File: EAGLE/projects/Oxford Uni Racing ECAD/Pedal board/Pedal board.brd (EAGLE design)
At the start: 165.1 x 216.8 mm, 42 parts, among them J1 T821108A1S100CEU, J2 T821108A1S100CEU, J3 T821108A1S100CEU, J4 T821108A1S100CEU, K1 RT444012, T1 BT169, X2 D-SUB9-H2M09ST

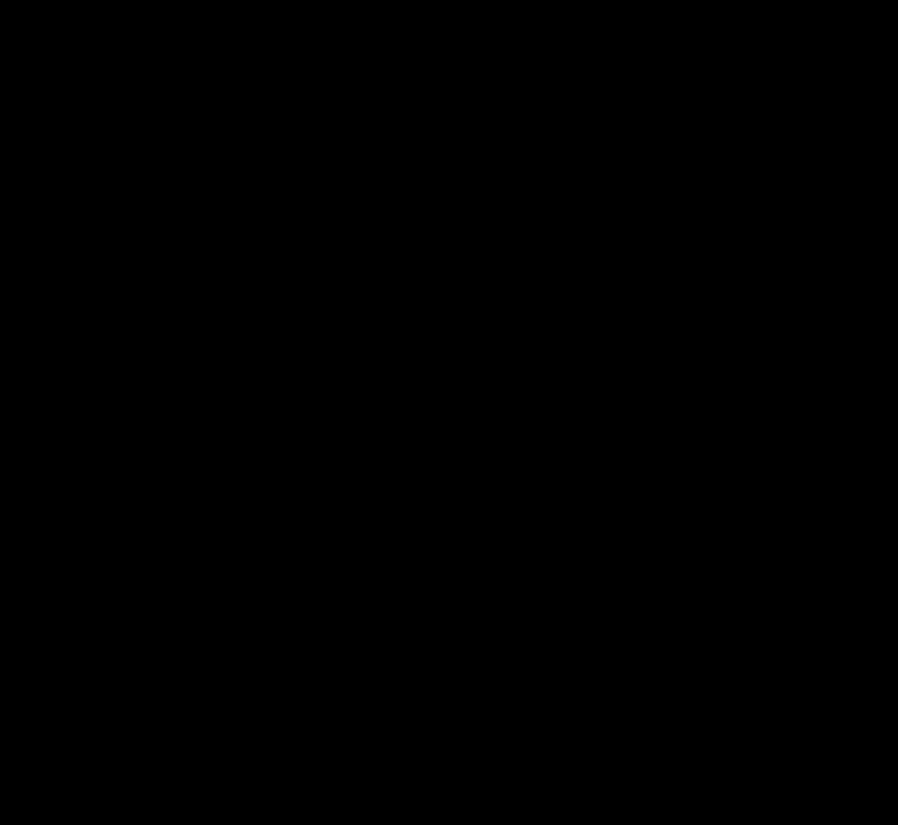
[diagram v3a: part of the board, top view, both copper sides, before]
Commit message: added outut connectors to the pedal board
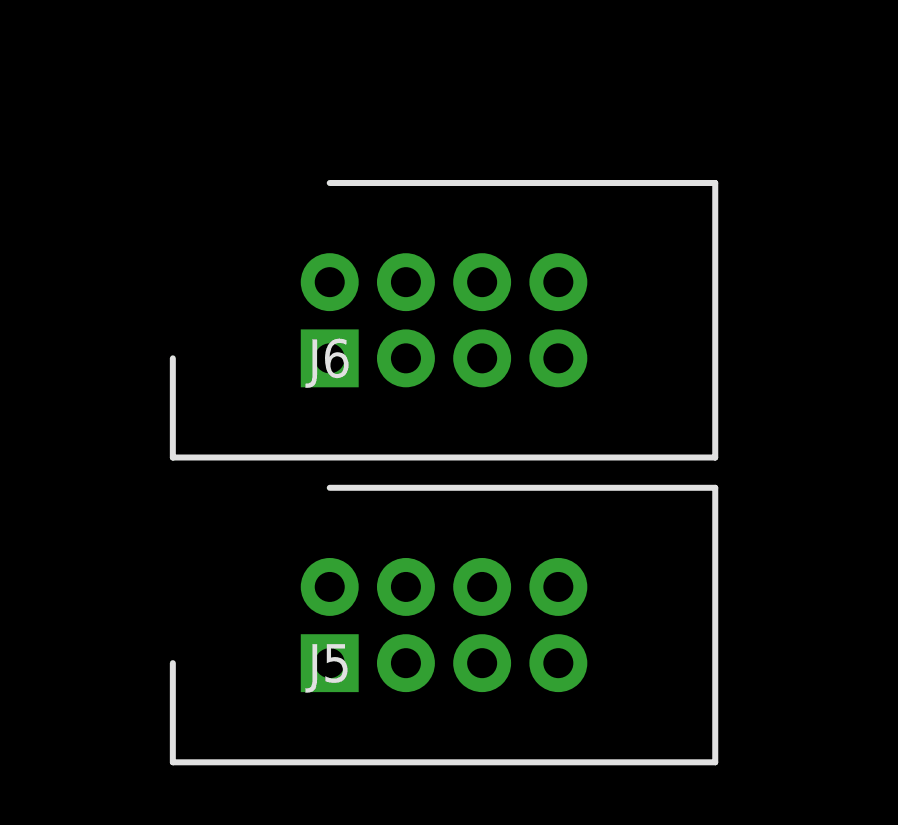
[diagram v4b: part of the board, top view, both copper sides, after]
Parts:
- added J5, J6: T821108A1S100CEU, T821108A1S100CEU:HDRV8W64P254_2X4_1778X895X915P
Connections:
- net CAN_H renamed CANH
- net CAN_L renamed CANL
- new net BRAKE_LIGHT_PWR_OUT: J5.8
- new net BR_POSS: J6.5
- new net BR_PRESS: J6.6
- new net ST_WH_POSS: J6.7
- net 3.3V: now also J6.1
- net 5V: now also J6.2
- net GND: now also J5.3, J6.3
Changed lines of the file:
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@@
 <attribute name="VALUE" x="149.86" y="43.18" size="1.27" layer="27" align="center"/>
+</element>
+<element name="J6" library="T821108A1S100CEU" package="HDRV8W64P254_2X4_1778X895X915P" value="T821108A1S100CEU" x="8.89" y="-120.65" smashed="yes">
+<attribute name="DESCRIPTION" value="HEADER, VERTICAL, 2.54MM, 8WAY Amphenol T821 Series, 2.54mm Pitch 8 Way 2 Row Straight PCB Header, Solder Termination, 3A" x="6.35" y="-120.65" size="1.778" layer="27" display="off"/>
+<attribute name="HEIGHT" value="9.15mm" x="6.35" y="-120.65" size="1.778" layer="27" display="off"/>
+<attribute name="MANUFACTURER_NAME" value="Amphenol" x="6.35" y="-120.65" size="1.778" layer="27" display="off"/>
+<attribute name="MANUFACTURER_PART_NUMBER" value="T821108A1S100CEU" x="6.35" y="-120.65" size="1.778" layer="27" display="off"/>
+<attribute name="NAME" x="8.89" y="-120.65" size="1.27" layer="25" align="center"/>
+<attribute name="RS_PART_NUMBER" value="1702738" x="6.35" y="-120.65" size="1.778" layer="27" display="off"/>
+<attribute name="VALUE" x="8.89" y="-120.65" size="1.27" layer="27" align="center"/>
+</element>
+<element name="J5" library="T821108A1S100CEU" package="HDRV8W64P254_2X4_1778X895X915P" value="T821108A1S100CEU" x="8.89" y="-130.81" smashed="yes">
+<attribute name="DESCRIPTION" value="HEADER, VERTICAL, 2.54MM, 8WAY Amphenol T821 Series, 2.54mm Pitch 8 Way 2 Row Straight PCB Header, Solder Termination, 3A" x="6.35" y="-130.81" size="1.778" layer="27" display="off"/>
+<attribute name="HEIGHT" value="9.15mm" x="6.35" y="-130.81" size="1.778" layer="27" display="off"/>
+<attribute name="MANUFACTURER_NAME" value="Amphenol" x="6.35" y="-130.81" size="1.778" layer="27" display="off"/>
+<attribute name="MANUFACTURER_PART_NUMBER" value="T821108A1S100CEU" x="6.35" y="-130.81" size="1.778" layer="27" display="off"/>
+<attribute name="NAME" x="8.89" y="-130.81" size="1.27" layer="25" align="center"/>
+<attribute name="RS_PART_NUMBER" value="1702738" x="6.35" y="-130.81" size="1.778" layer="27" display="off"/>
+<attribute name="VALUE" x="8.89" y="-130.81" size="1.27" layer="27" align="center"/>
 </element>
 </elements>
@@
 <contactref element="J2" pad="4"/>
 <contactref element="J4" pad="3"/>
+<contactref element="J6" pad="3"/>
+<contactref element="J5" pad="3"/>
+<wire x1="149.86" y1="36.83" x2="149.86" y2="45.72" width="0" layer="19" extent="1-1"/>
+<wire x1="149.86" y1="34.29" x2="149.86" y2="36.83" width="0" layer="19" extent="1-1"/>
+<wire x1="134.62" y1="22.86" x2="149.86" y2="34.29" width="0" layer="19" extent="16-16"/>
 <wire x1="111.76" y1="17.78" x2="125.73" y2="10.16" width="0" layer="19" extent="16-16"/>
-<wire x1="87.63" y1="22.86" x2="102.87" y2="10.16" width="0" layer="19" extent="16-16"/>
+<wire x1="91.44" y1="11.43" x2="102.87" y2="10.16" width="0" layer="19" extent="16-16"/>
 <wire x1="20.6502" y1="-29.72970625" x2="82.55" y2="8.7376" width="0" layer="19" extent="16-16"/>
 <wire x1="19.124928125" y1="-63.86195" x2="19.3294" y2="-37.5412" width="0" layer="19" extent="1-1"/>
 <wire x1="12.75714375" y1="-86.45144375" x2="13.55979375" y2="-86.45144375" width="0" layer="19" extent="16-16"/>
-<wire x1="149.86" y1="36.83" x2="24.63165" y2="-97.547428125" width="0" layer="19" extent="1-1"/>
-<wire x1="149.86" y1="34.29" x2="149.86" y2="36.83" width="0" layer="19" extent="1-1"/>
-<wire x1="149.86" y1="45.72" x2="149.86" y2="34.29" width="0" layer="19" extent="1-1"/>
+<wire x1="11.43" y1="-120.65" x2="24.63165" y2="-97.547428125" width="0" layer="19" extent="1-1"/>
+<wire x1="11.43" y1="-130.81" x2="11.43" y2="-120.65" width="0" layer="19" extent="1-1"/>
 </signal>
 <signal name="N$3">
@@
 <wire x1="111.76" y1="7.62" x2="125.73" y2="7.62" width="0" layer="19" extent="16-16"/>
 <wire x1="90.17" y1="20.32" x2="102.87" y2="7.62" width="0" layer="19" extent="16-16"/>
-<wire x1="23.8506" y1="-31.0388" x2="90.17" y2="20.32" width="0" layer="19" extent="1-1"/>
-<wire x1="11.376653125" y1="-63.733675" x2="23.8506" y2="-31.0388" width="0" layer="19" extent="16-16"/>
-</signal>
-<signal name="CAN_L">
+<wire x1="71.11193125" y1="-68.1202625" x2="102.87" y2="7.62" width="0" layer="19" extent="16-16"/>
+<wire x1="23.8506" y1="-31.0388" x2="11.376653125" y2="-63.733675" width="0" layer="19" extent="16-16"/>
+</signal>
+<signal name="CANL">
 <contactref element="X2" pad="2"/>
 <wire x1="85.09" y1="14.7717375" x2="85.21065" y2="14.6510875" width="0.6096" layer="16"/>
@@
 <wire x1="85.09" y1="20.32" x2="85.09" y2="22.86" width="0" layer="19" extent="1-1"/>
 </signal>
-<signal name="CAN_H">
+<signal name="CANH">
 <contactref element="X2" pad="7"/>
 <wire x1="83.9343" y1="11.5824" x2="82.55" y2="12.9667" width="1.27" layer="16"/>
@@
 <wire x1="137.16" y1="21.59" x2="137.16" y2="22.86" width="1.27" layer="16"/>
 <wire x1="139.7" y1="21.59" x2="137.16" y2="21.59" width="1.27" layer="16"/>
-<wire x1="78.3971" y1="11.5824" x2="137.16" y2="7.62" width="0" layer="19" extent="1-1"/>
+<contactref element="J6" pad="2"/>
+<wire x1="78.3971" y1="11.5824" x2="137.16" y2="15.24" width="0" layer="19" extent="1-1"/>
+<wire x1="8.89" y1="-118.11" x2="78.3971" y2="11.5824" width="0" layer="19" extent="1-1"/>
 </signal>
 <signal name="N$24">
@@
 <wire x1="114.3" y1="21.59" x2="114.3" y2="22.86" width="1.27" layer="16"/>
 <wire x1="116.84" y1="21.59" x2="114.3" y2="21.59" width="1.27" layer="16"/>
-<wire x1="147.32" y1="36.83" x2="114.3" y2="7.62" width="0" layer="19" extent="1-1"/>
+<contactref element="J6" pad="1"/>
+<wire x1="147.32" y1="36.83" x2="147.32" y2="45.72" width="0" layer="19" extent="1-1"/>
 <wire x1="147.32" y1="34.29" x2="147.32" y2="36.83" width="0" layer="19" extent="1-1"/>
-<wire x1="147.32" y1="45.72" x2="147.32" y2="34.29" width="0" layer="19" extent="1-1"/>
+<wire x1="116.84" y1="21.59" x2="147.32" y2="34.29" width="0" layer="19" extent="1-1"/>
+<wire x1="8.89" y1="-120.65" x2="114.3" y2="7.62" width="0" layer="19" extent="1-1"/>
+</signal>
+<signal name="BR_POSS">
+<contactref element="J6" pad="5"/>
+</signal>
+<signal name="BR_PRESS">
+<contactref element="J6" pad="6"/>
+</signal>
+<signal name="ST_WH_POSS">
+<contactref element="J6" pad="7"/>
+</signal>
+<signal name="BRAKE_LIGHT_PWR_OUT">
+<contactref element="J5" pad="8"/>
 </signal>
 </signals>

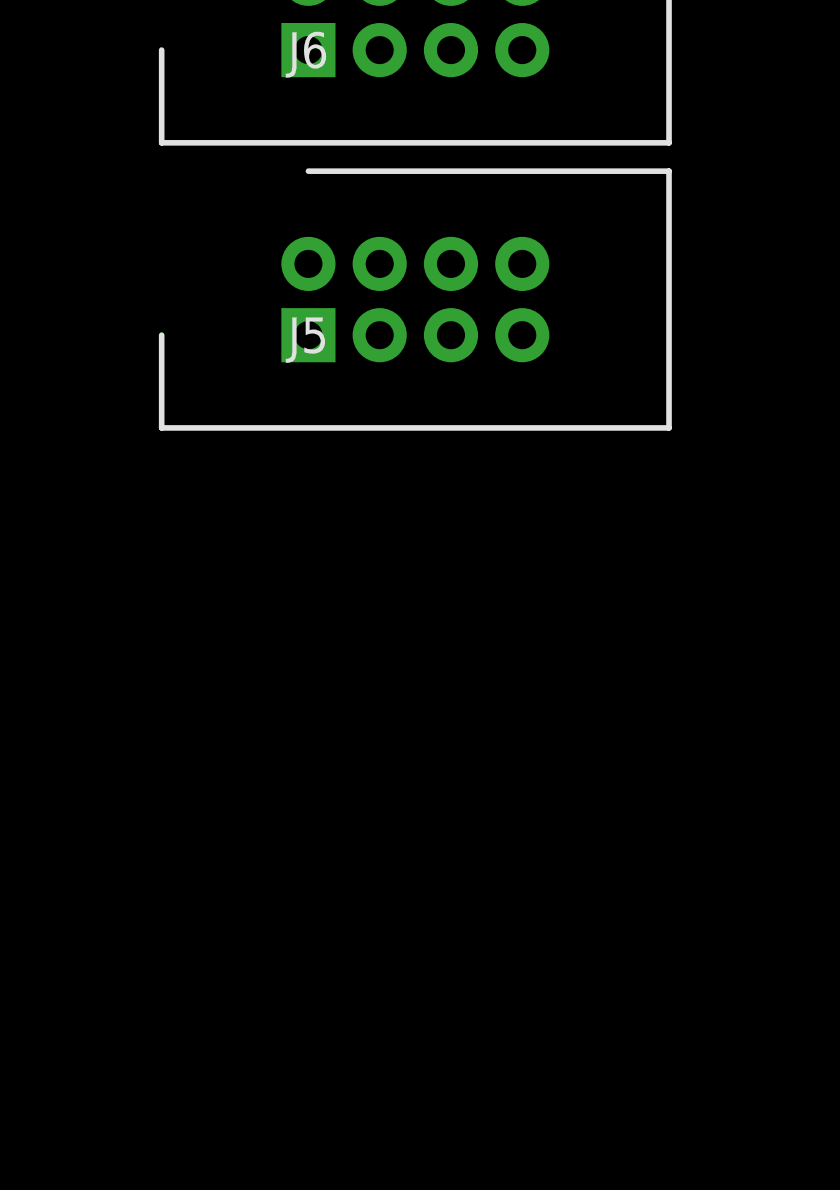
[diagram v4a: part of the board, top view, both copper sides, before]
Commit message: added brake out to pedal board
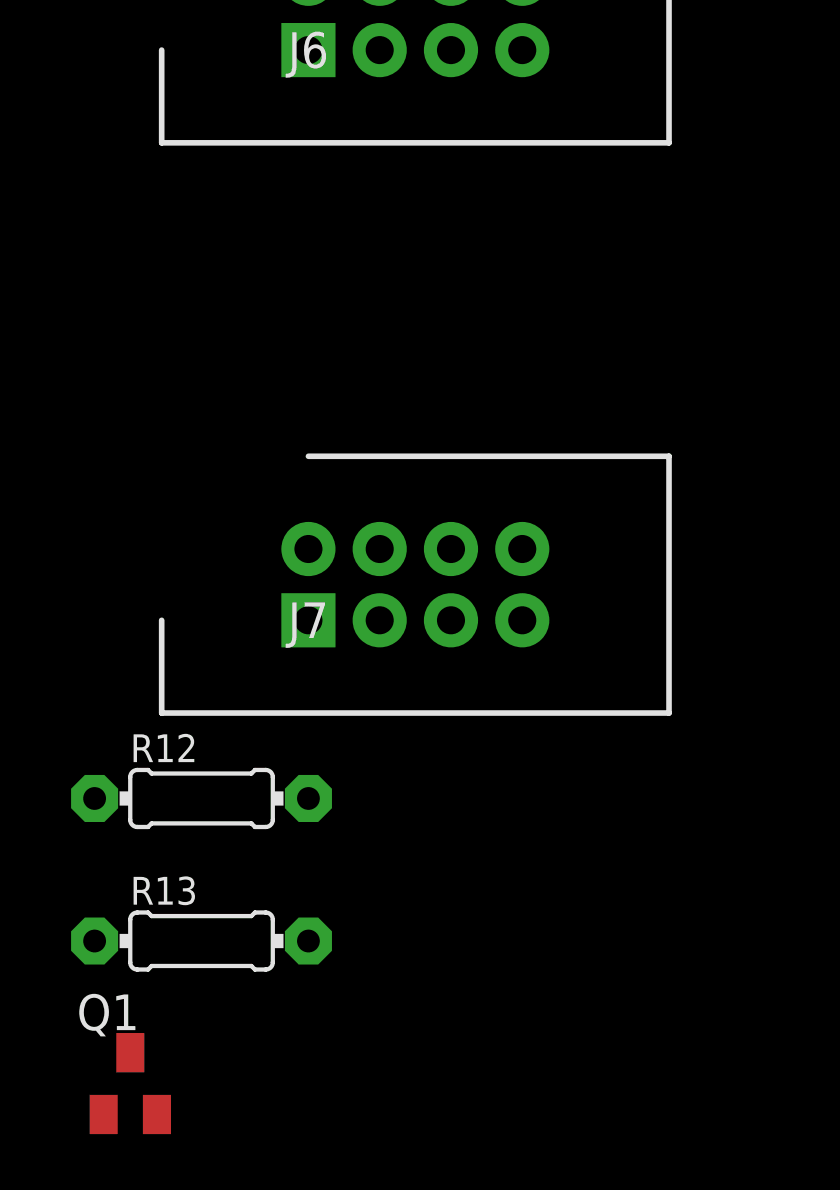
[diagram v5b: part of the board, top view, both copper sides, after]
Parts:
- removed J5: T821108A1S100CEU, T821108A1S100CEU:HDRV8W64P254_2X4_1778X895X915P
- added J7: T821108A1S100CEU, T821108A1S100CEU:HDRV8W64P254_2X4_1778X895X915P
- added Q1: (no value), adafruit:SOT23
- added R12: 1K, adafruit:0204/7
- added R13: 47K, adafruit:0204/7
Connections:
- removed net BRAKE_LIGHT_PWR_OUT: J5.8
- new net BRAKE_LIGHTS_OUT: R12.1
- new net N$25: Q1.1, R12.2, R13.2
- new net N$28: J7.3, Q1.3
- net 12V: now also J7.8
- net GND: now also Q1.2, R13.1; no longer J5.3
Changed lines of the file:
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@@
 <attribute name="VALUE" x="8.89" y="-120.65" size="1.27" layer="27" align="center"/>
 </element>
-<element name="J5" library="T821108A1S100CEU" package="HDRV8W64P254_2X4_1778X895X915P" value="T821108A1S100CEU" x="8.89" y="-130.81" smashed="yes">
-<attribute name="DESCRIPTION" value="HEADER, VERTICAL, 2.54MM, 8WAY Amphenol T821 Series, 2.54mm Pitch 8 Way 2 Row Straight PCB Header, Solder Termination, 3A" x="6.35" y="-130.81" size="1.778" layer="27" display="off"/>
-<attribute name="HEIGHT" value="9.15mm" x="6.35" y="-130.81" size="1.778" layer="27" display="off"/>
-<attribute name="MANUFACTURER_NAME" value="Amphenol" x="6.35" y="-130.81" size="1.778" layer="27" display="off"/>
-<attribute name="MANUFACTURER_PART_NUMBER" value="T821108A1S100CEU" x="6.35" y="-130.81" size="1.778" layer="27" display="off"/>
-<attribute name="NAME" x="8.89" y="-130.81" size="1.27" layer="25" align="center"/>
-<attribute name="RS_PART_NUMBER" value="1702738" x="6.35" y="-130.81" size="1.778" layer="27" display="off"/>
-<attribute name="VALUE" x="8.89" y="-130.81" size="1.27" layer="27" align="center"/>
+<element name="J7" library="T821108A1S100CEU" package="HDRV8W64P254_2X4_1778X895X915P" value="T821108A1S100CEU" x="8.89" y="-140.97" smashed="yes">
+<attribute name="DESCRIPTION" value="HEADER, VERTICAL, 2.54MM, 8WAY Amphenol T821 Series, 2.54mm Pitch 8 Way 2 Row Straight PCB Header, Solder Termination, 3A" x="6.35" y="-140.97" size="1.778" layer="27" display="off"/>
+<attribute name="HEIGHT" value="9.15mm" x="6.35" y="-140.97" size="1.778" layer="27" display="off"/>
+<attribute name="MANUFACTURER_NAME" value="Amphenol" x="6.35" y="-140.97" size="1.778" layer="27" display="off"/>
+<attribute name="MANUFACTURER_PART_NUMBER" value="T821108A1S100CEU" x="6.35" y="-140.97" size="1.778" layer="27" display="off"/>
+<attribute name="NAME" x="8.89" y="-140.97" size="1.27" layer="25" align="center"/>
+<attribute name="RS_PART_NUMBER" value="1702738" x="6.35" y="-140.97" size="1.778" layer="27" display="off"/>
+<attribute name="VALUE" x="8.89" y="-140.97" size="1.27" layer="27" align="center"/>
+</element>
+<element name="R12" library="adafruit" library_urn="urn:adsk.eagle:library:420" package="0204/7" package3d_urn="urn:adsk.eagle:package:6240596/1" value="1K" x="5.08" y="-147.32" smashed="yes">
+<attribute name="NAME" x="2.54" y="-146.0246" size="0.9906" layer="25" ratio="12"/>
+<attribute name="VALUE" x="3.4544" y="-147.8026" size="0.9906" layer="27" ratio="12"/>
+</element>
+<element name="R13" library="adafruit" library_urn="urn:adsk.eagle:library:420" package="0204/7" package3d_urn="urn:adsk.eagle:package:6240596/1" value="47K" x="5.08" y="-152.4" smashed="yes">
+<attribute name="NAME" x="2.54" y="-151.1046" size="0.9906" layer="25" ratio="12"/>
+<attribute name="VALUE" x="3.4544" y="-152.8826" size="0.9906" layer="27" ratio="12"/>
+</element>
+<element name="Q1" library="adafruit" library_urn="urn:adsk.eagle:library:420" package="SOT23" package3d_urn="urn:adsk.eagle:package:6240836/1" value="" x="2.54" y="-157.48" smashed="yes">
+<attribute name="NAME" x="0.635" y="-155.575" size="1.27" layer="25"/>
+<attribute name="VALUE" x="0.635" y="-160.655" size="1.27" layer="27"/>
 </element>
 </elements>
@@
 <contactref element="J4" pad="3"/>
 <contactref element="J6" pad="3"/>
-<contactref element="J5" pad="3"/>
+<contactref element="R13" pad="1"/>
+<contactref element="Q1" pad="2"/>
 <wire x1="149.86" y1="36.83" x2="149.86" y2="45.72" width="0" layer="19" extent="1-1"/>
 <wire x1="149.86" y1="34.29" x2="149.86" y2="36.83" width="0" layer="19" extent="1-1"/>
@@
 <wire x1="12.75714375" y1="-86.45144375" x2="13.55979375" y2="-86.45144375" width="0" layer="19" extent="16-16"/>
 <wire x1="11.43" y1="-120.65" x2="24.63165" y2="-97.547428125" width="0" layer="19" extent="1-1"/>
-<wire x1="11.43" y1="-130.81" x2="11.43" y2="-120.65" width="0" layer="19" extent="1-1"/>
+<wire x1="1.27" y1="-152.4" x2="11.43" y2="-120.65" width="0" layer="19" extent="1-1"/>
+<wire x1="3.49" y1="-158.58" x2="1.27" y2="-152.4" width="0" layer="19" extent="1-1"/>
 </signal>
 <signal name="N$3">
@@
 <wire x1="134.62" y1="7.62" x2="129.54" y2="7.62" width="1.27" layer="16"/>
 <wire x1="129.54" y1="7.62" x2="125.73" y2="7.62" width="1.27" layer="16"/>
+<contactref element="J7" pad="8"/>
 <wire x1="111.76" y1="7.62" x2="125.73" y2="7.62" width="0" layer="19" extent="16-16"/>
 <wire x1="90.17" y1="20.32" x2="102.87" y2="7.62" width="0" layer="19" extent="16-16"/>
 <wire x1="71.11193125" y1="-68.1202625" x2="102.87" y2="7.62" width="0" layer="19" extent="16-16"/>
 <wire x1="23.8506" y1="-31.0388" x2="11.376653125" y2="-63.733675" width="0" layer="19" extent="16-16"/>
+<wire x1="16.51" y1="-138.43" x2="8.8866375" y2="-98.7666375" width="0" layer="19" extent="16-16"/>
 </signal>
 <signal name="CANL">
@@
 <contactref element="J6" pad="7"/>
 </signal>
-<signal name="BRAKE_LIGHT_PWR_OUT">
-<contactref element="J5" pad="8"/>
+<signal name="BRAKE_LIGHTS_OUT">
+<contactref element="R12" pad="1"/>
+</signal>
+<signal name="N$25">
+<contactref element="R12" pad="2"/>
+<contactref element="R13" pad="2"/>
+<contactref element="Q1" pad="1"/>
+<wire x1="8.89" y1="-152.4" x2="1.59" y2="-158.58" width="0" layer="19" extent="1-1"/>
+<wire x1="8.89" y1="-147.32" x2="8.89" y2="-152.4" width="0" layer="19" extent="1-1"/>
+</signal>
+<signal name="N$28">
+<contactref element="J7" pad="3"/>
+<contactref element="Q1" pad="3"/>
+<wire x1="11.43" y1="-140.97" x2="2.54" y2="-156.38" width="0" layer="19" extent="1-1"/>
 </signal>
 </signals>
